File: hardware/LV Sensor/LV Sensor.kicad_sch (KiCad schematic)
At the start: 64 parts, among them J1 Conn_01x04_Pin, J2 Conn_01x02_Pin, J3 TH, J4 SCREW, J5 TH, J6 SCREW, J7 Conn_01x02_Pin, SW1 SW_Push, U1 MSPM0G3507 RHB32, U10 DXTN80100CFGQ, U2 ISO1042BDW, U3 KA78M05_TO252, U4 KA78M05_TO252, U5 L78L33_SO8, U7 HBDM60V600X, U9 DXTN80100CFGQ

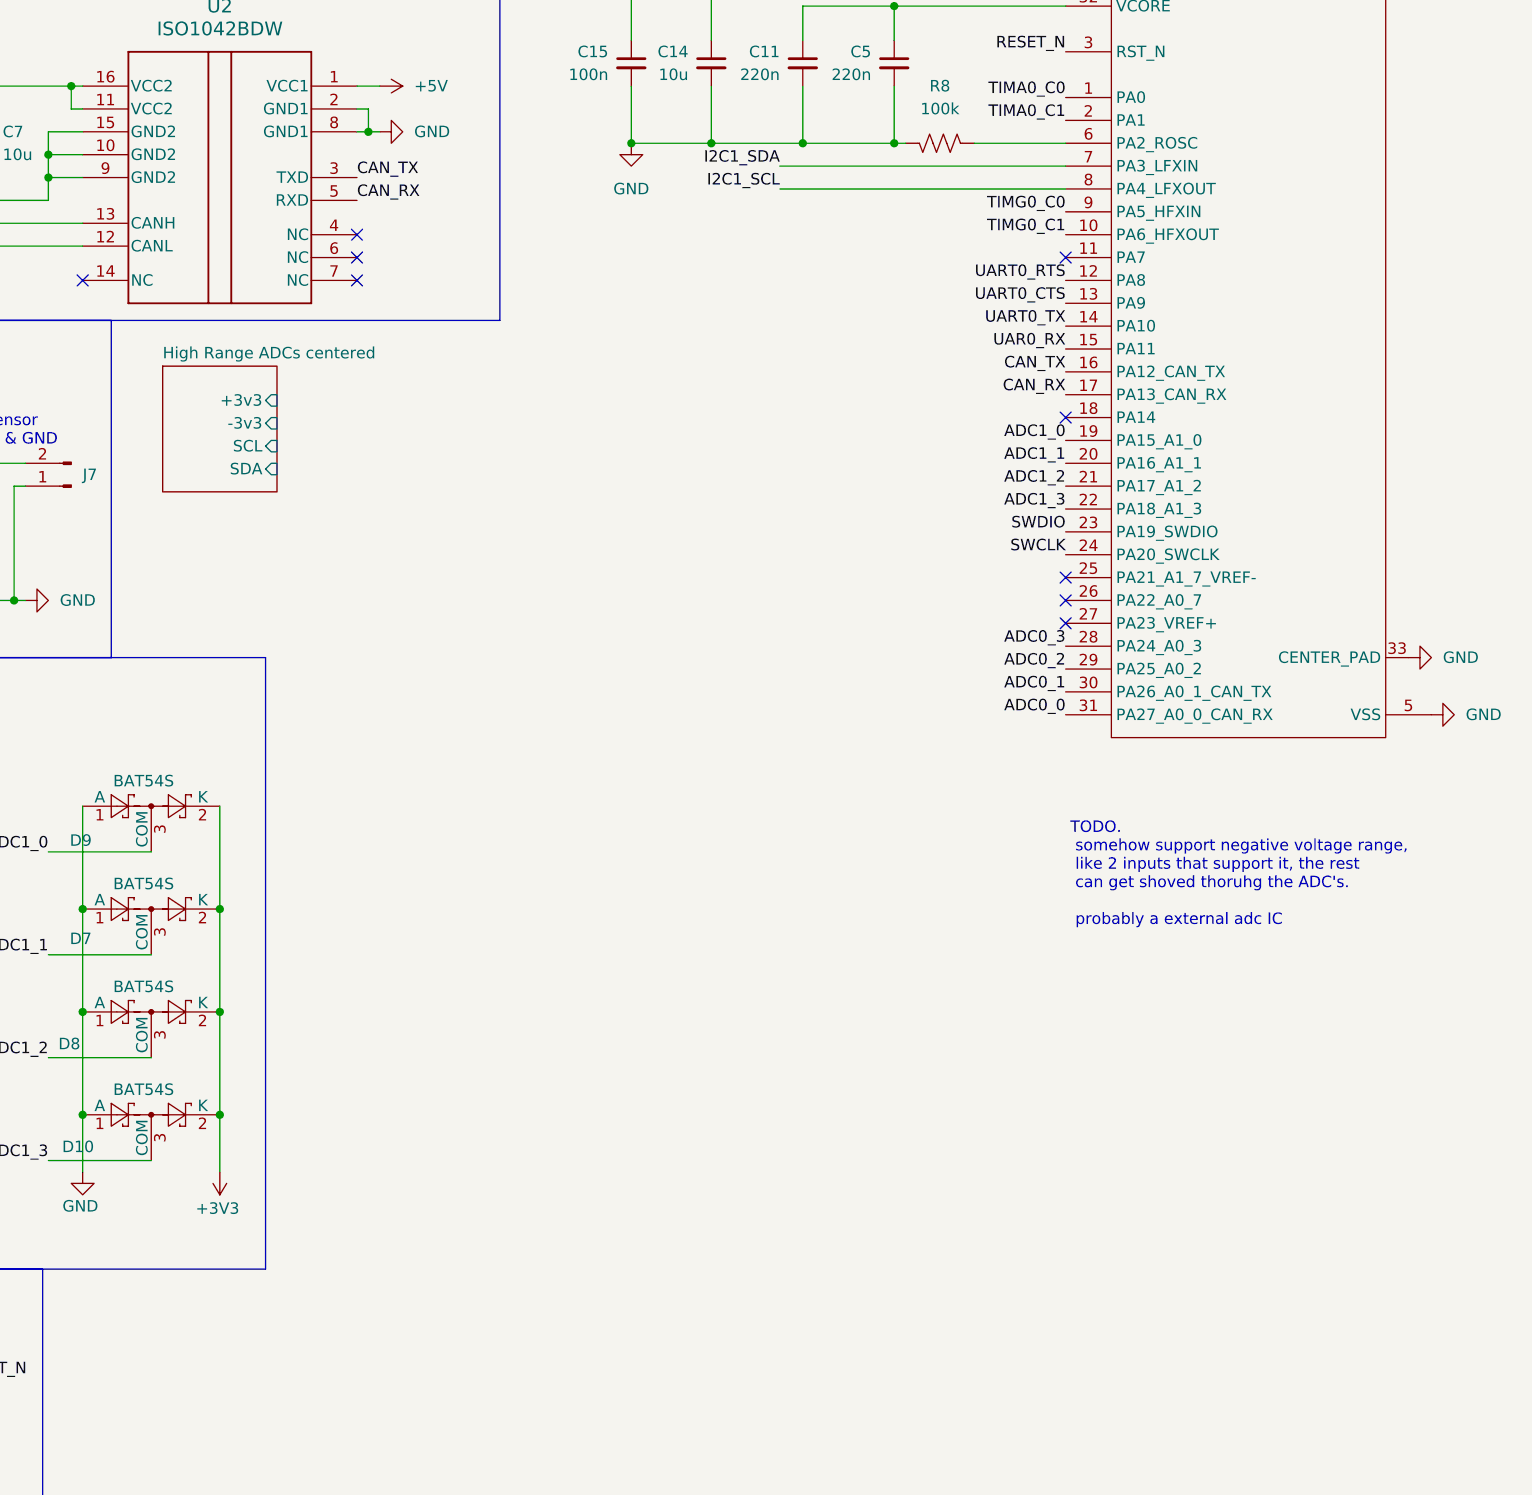
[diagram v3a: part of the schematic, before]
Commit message: noteed TODOs on LV sensor board
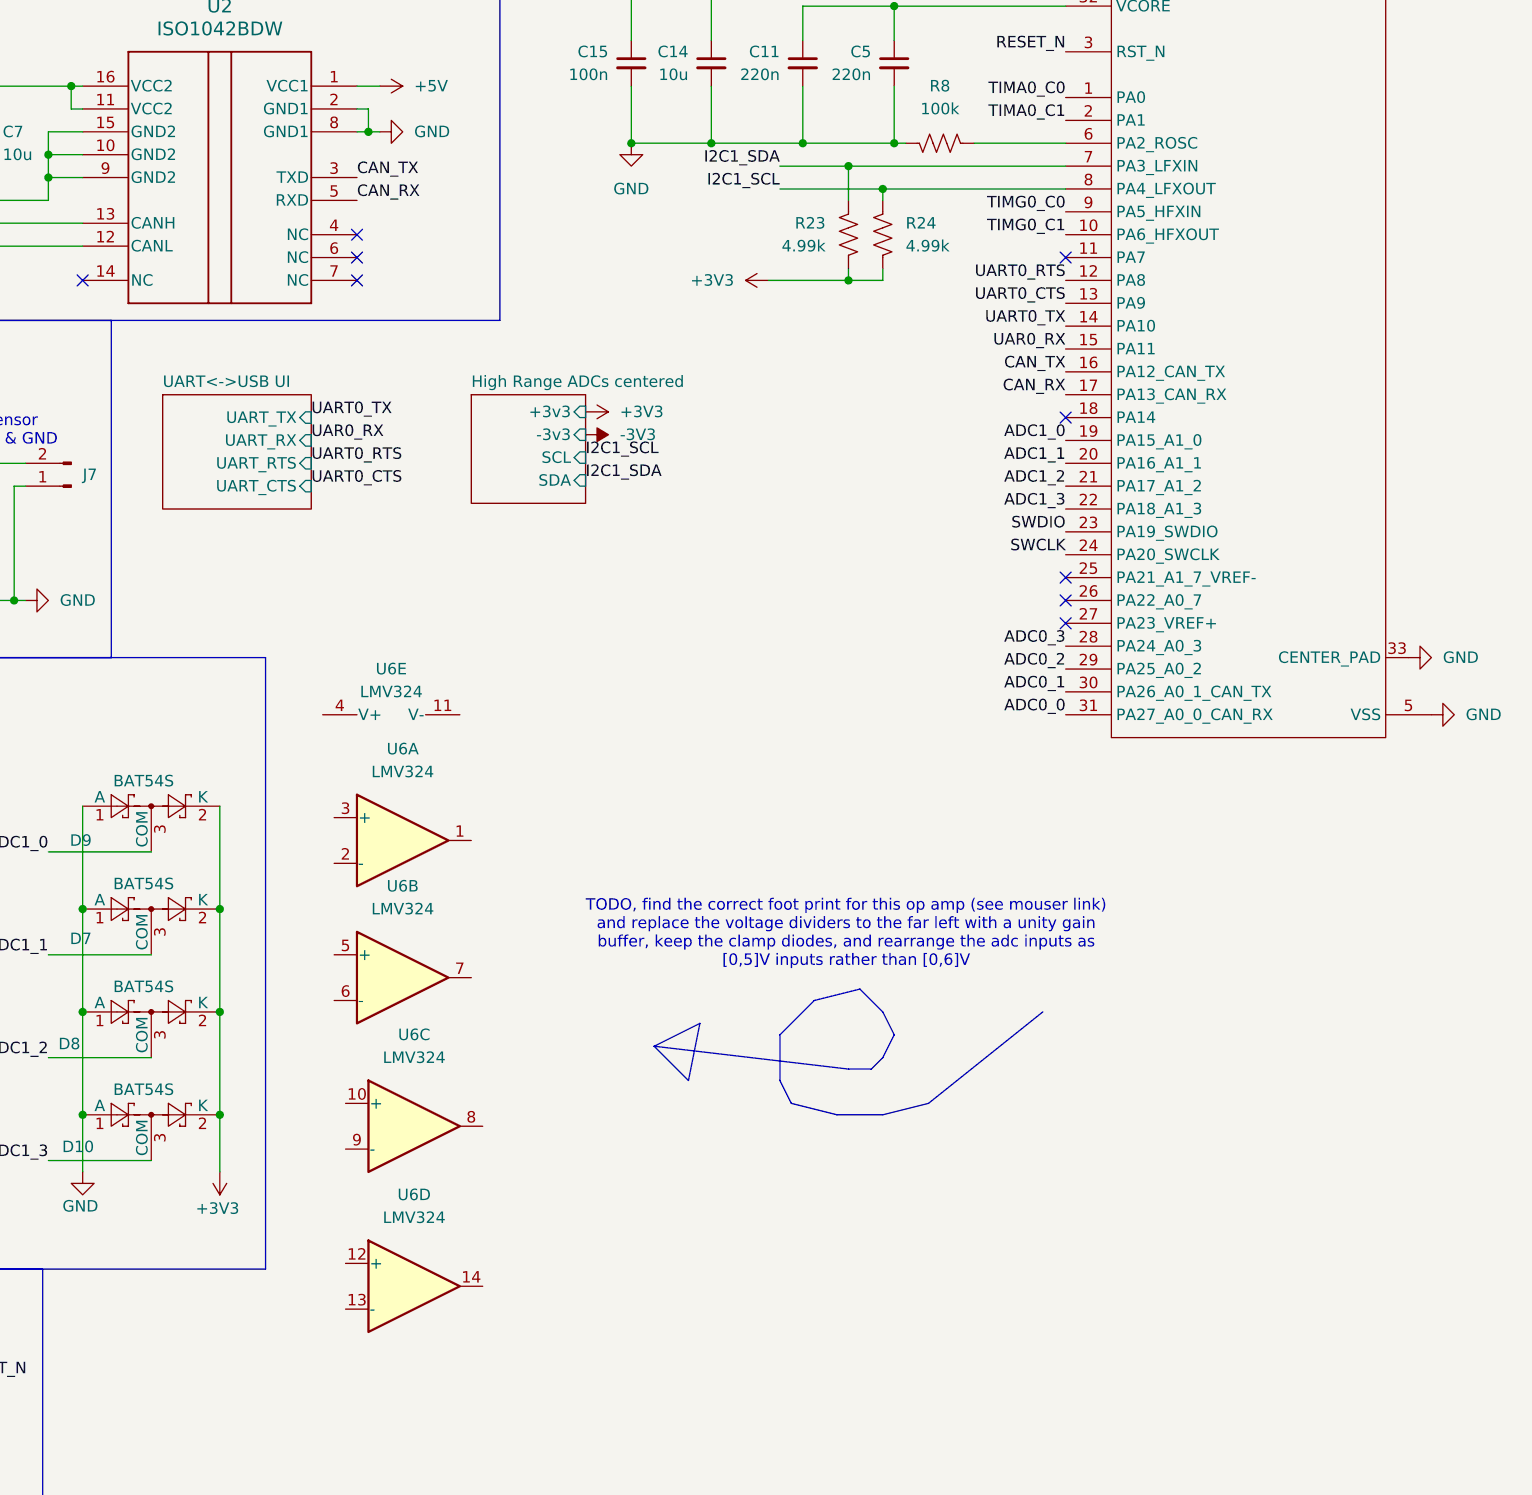
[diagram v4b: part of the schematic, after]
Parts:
- added R23, R24: 4.99k, Resistor_SMD:R_1206_3216Metric_Pad1.30x1.75mm_HandSolder, symbol Device:R_US
- added U6: LMV324, symbol Amplifier_Operational:LMV324
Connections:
- net +3V3: now also R23.1, R24.2
- net I2C1_SCL: now also R24.1
- net I2C1_SDA: now also R23.2
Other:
- added sheet UART<->USB UI (uart usb UI ftx based.kicad_sch)
- note added: "TODO, find the correct foot print for this op amp (see mouser link) and replace the voltage dividers to the far left with a unity gain buffer, keep the clamp diodes, and rearrange the adc inputs as [0,5]V inputs rather than [0,6]V"
- note removed: "TODO. somehow support negative voltage range, like 2 inputs that support it, the rest can get shoved thoruhg the ADC's. probably a external adc IC"

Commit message: more TODO notes
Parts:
- added J8: PWM signal connectors, symbol Connector_Generic:Conn_02x04_Counter_Clockwise
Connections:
- net +3V3: now also J8.1 (Pin_1)
- net +5V: now also J8.2 (Pin_2)
- net -BATT: now also J8.3 (Pin_3)
- net TIMA0_C0: now also J8.7 (Pin_7)
- net TIMA0_C1: now also J8.8 (Pin_8)
- net TIMG0_C0: now also J8.5 (Pin_5)
- net TIMG0_C1: now also J8.6 (Pin_6)
- no-connect marks 9 -> 10
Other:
- note added: "TODO: this board needs 1 h bridge to drive the DC fans, either copy the one from the linked repo, make your own, or find one elsewhere. its ~3 a 12V to 24V motors, up to 120W each, ask george about heat sinks if needed. use the timers attached to J8, either all 4 or just 2; C1 and C0 are different compare values on the same timer https://github.com/gregclacker/FourWheelSteering/tree/speedrun/KiCA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"

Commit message: bluhhh
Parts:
- removed J5: TH, Connector_PinHeader_2.54mm:PinHeader_1x04_P2.54mm_Vertical, symbol Connector:Conn_01x04_Pin
- removed J6: SCREW, TerminalBlock:TerminalBlock_MaiXu_MX126-5.0-04P_1x04_P5.00mm, symbol Connector:Conn_01x04_Pin
- removed R12, R13, R14, R15, R16, R17, R18, R19, R20, R21, R22: 100k, symbol Device:R_Small_US
- R10, R5, R6, R9: footprint (none) -> Resistor_SMD:R_1206_3216Metric_Pad1.30x1.75mm_HandSolder
- R11: value 100k -> 50k; footprint (none) -> Resistor_SMD:R_1206_3216Metric_Pad1.30x1.75mm_HandSolder; mouser https://www.mouser.com/ProductDetail/YAGEO/RC1206FR-07100KL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 -> https://www.mouser.com/ProductDetail/YAGEO/RT1206BRD0750KL?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; unit x1 0.10 -> 0.21; unit x10 0.016 -> 0.161
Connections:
- net +3V3: no longer D11.2 (K), D12.2 (K), D13.2 (K), D14.2 (K)
- net +5V: now also D11.2 (K), D12.2 (K), D13.2 (K), D14.2 (K), U6.4 (V+)
- net -BATT: now also U6.11 (V-); no longer R11.1
- net ADC0_0: now also U6.1; no longer D11.3 (COM), R5.2
- net ADC0_1: no longer D12.3 (COM), R6.2
- net ADC0_2: no longer D13.3 (COM), R9.2
- net ADC0_3: no longer D14.3 (COM), R10.2
- net at J3.3 (Pin_3), J4.3 (Pin_3): no longer R9.1
- net at J3.2 (Pin_2), J4.2 (Pin_2): no longer R6.1
- net at J3.4 (Pin_4), J4.4 (Pin_4): no longer R10.1
- net at J3.1 (Pin_1), J4.1 (Pin_1): no longer R5.1
- net at U6.2 (-): now also R11.1
- new net: D11.3 (COM), R9.2
- new net: D13.3 (COM), R5.2
- new net: D14.3 (COM), R10.2
- new net: D12.3 (COM), R6.2
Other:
- note added: "[0,5]V ADC input 11b to 14b - direct to MCU. 11b res."
- note removed: "[0,6]V ADC input 11b to 14b - direct to MCU. 11b res."
- moved on the sheet: D10, D11, D12, D13, D14, D7, D8, D9, R10, U6A, U6C, U6D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

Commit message: adln
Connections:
- net at R9.1: now also J3.1 (Pin_1), J4.1 (Pin_1)
- net at R5.1: now also J3.3 (Pin_3), J4.3 (Pin_3)
- net at R10.1: now also J3.4 (Pin_4), J4.4 (Pin_4)
- net at J3.2 (Pin_2), J4.2 (Pin_2): now also R6.1
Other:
- moved on the sheet: D11, D12, D13, D14, J3, J4, R10, R5, R6, R9
